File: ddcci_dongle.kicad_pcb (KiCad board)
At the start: 4 copper layers, 31 x 64 mm, 52 parts, among them U1 PCA9306, U10 TPD1E05U06DPY, U11 TPD1E05U06DPY, U12 TPD1E05U06DPY, U2 NCP1117-3.3_SOT223, U3 RP2040, U4 W25Q128JVPIQ, U6 TPD1E05U06DPY, U8 TPD1E05U06DPY, U9 TPD1E05U06DPY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

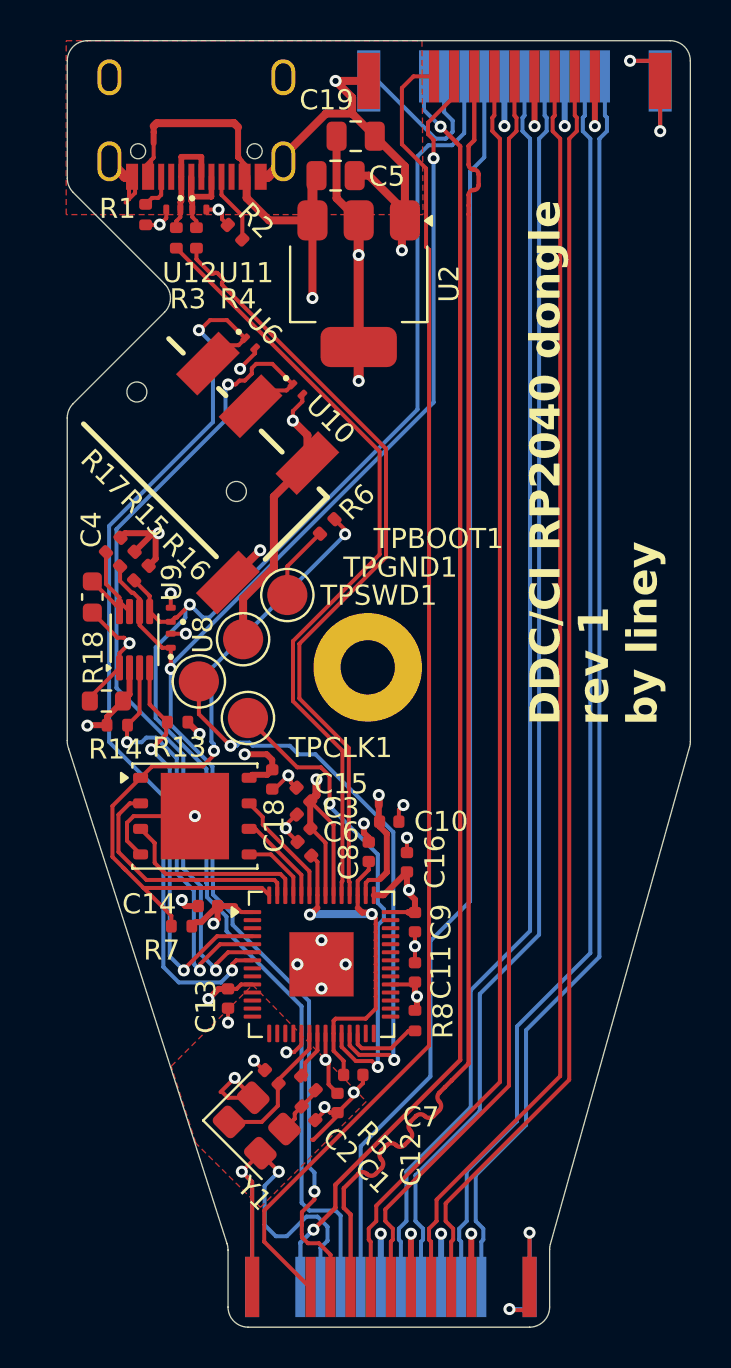
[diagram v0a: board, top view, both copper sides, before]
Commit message: Final update before rev1 production
* Update LCSC PN# fields
* Add ground to layer 3 (3.3v has been reduced to a polygon)
* Remove the antennas on the right (behind HDMI lanes)
* Remove the ground plane "capacitor" under the XTAL
* Prettier testpoint labels
* Prettier tracks overall

Signed-off-by: Elvira Khabirova <lineprinter0@gmail.com>
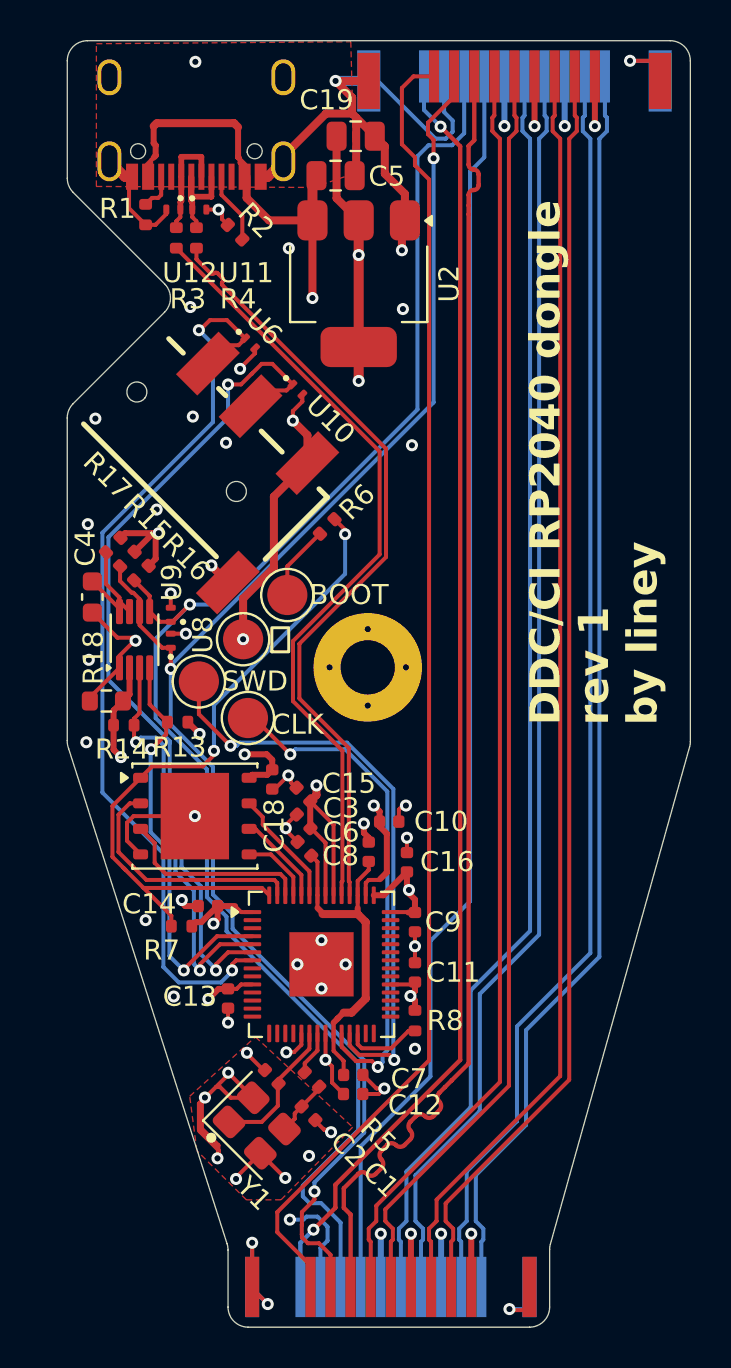
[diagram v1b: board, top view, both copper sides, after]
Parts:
- moved C12 0.90 mm to (126.2, 125.8), turned to 0 degrees
- moved R14 0.32 mm to (114.8, 107.4)
- moved R5 0.25 mm to (124.2, 125.0)
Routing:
- net GND: track 132.8 -> 120.2 mm, vias 33 -> 56
- net +1V1: track 19.9 -> 17.1 mm, vias 2 -> 0
- net /DISPLAY_SCK: track 76.9 -> 78.9 mm
- net Net-(U3-SWCLK): track 23.9 -> 25.4 mm
- net /DISPLAY_SDA: track 77.8 -> 79.1 mm
- net Net-(U3-SWD): track 28.4 -> 29.6 mm
- net +3V3: track 59.4 -> 58.5 mm
- net Net-(HDMI1-+5VPower): track 66.4 -> 65.9 mm
- net /SHIFTED_DISPLAY_SCK: track 21.3 -> 20.8 mm
- added copper zone on In2.Cu, net GND
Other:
- board text added: "BOOT"
- board text added: "CLK"
- board text added: "SWD"
- board text added: "⏚"

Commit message: Fix SDA/SCL for the monitor. Bump to rev2
Signed-off-by: Elvira Khabirova <lineprinter0@gmail.com>
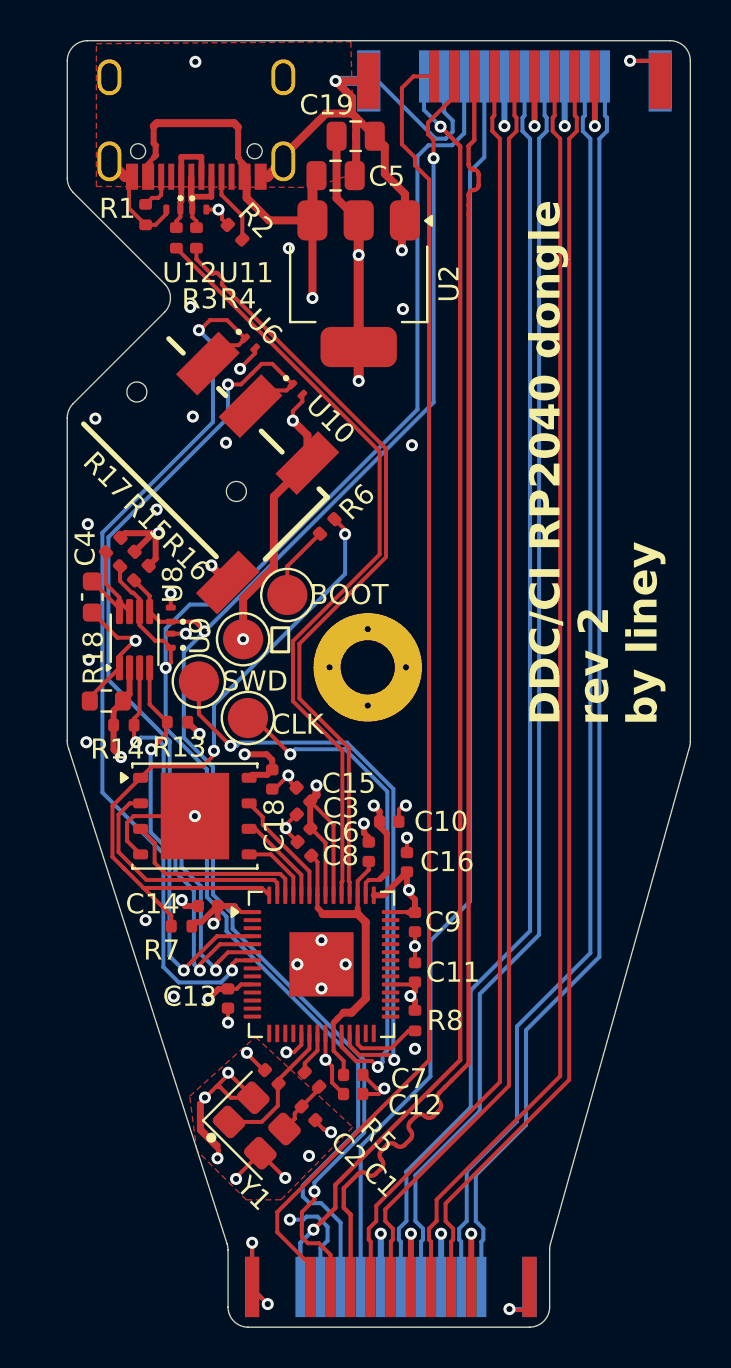
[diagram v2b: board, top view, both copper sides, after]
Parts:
- moved U8 1.30 mm to (117.2, 101.9)
- moved U9 1.29 mm to (117.2, 103.2)
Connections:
- HDMI1 pad 15: /DISPLAY_SDA -> /DISPLAY_SCK
- HDMI1 pad 16: /DISPLAY_SCK -> /DISPLAY_SDA
- U5 pad 15: /DISPLAY_SDA -> /DISPLAY_SCK
- U5 pad 16: /DISPLAY_SCK -> /DISPLAY_SDA
- U8 pad 1: /DISPLAY_SCK -> /DISPLAY_SDA
- U9 pad 1: /DISPLAY_SDA -> /DISPLAY_SCK
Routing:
- net /DISPLAY_SDA: track 79.1 -> 77.1 mm, vias 1 -> 3
- net /DISPLAY_SCK: track 78.9 -> 80.7 mm, vias 3 -> 1
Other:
- board text added: "DDC/CI RP2040 dongle rev 2 by liney"
- board text removed: "DDC/CI RP2040 dongle rev 1 by liney"

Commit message: WIP: Make the board narrower
Todo: make the board shorter

Signed-off-by: Elvira Khabirova <lineprinter0@gmail.com>
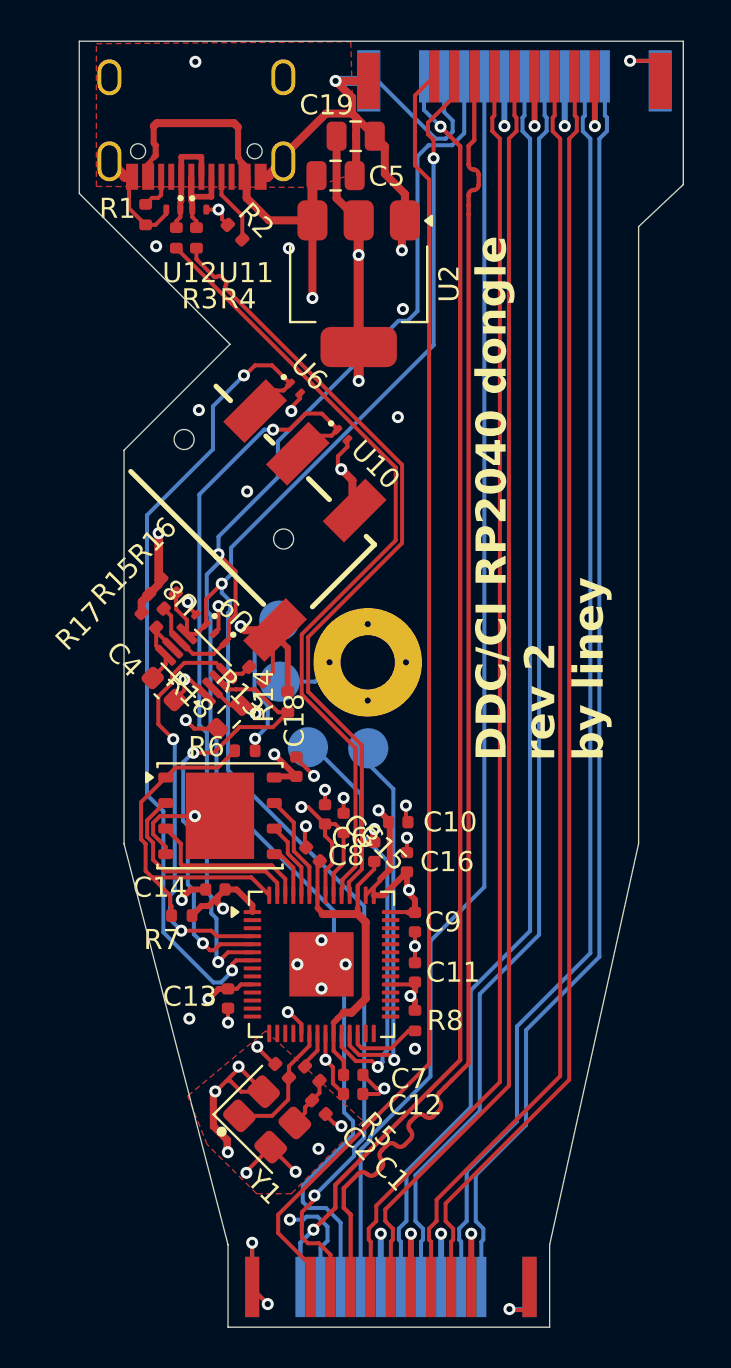
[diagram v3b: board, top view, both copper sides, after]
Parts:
- TPBOOT1, TPCLK1, TPGND1, TPSWD1: moved to B.Cu
- moved R6 11.9 mm to (120.8, 108.7), turned to 0 degrees
- moved TPSWD1 9.06 mm to (127.0, 108.5)
- moved R14 8.24 mm to (123.0, 106.2), turned to -90 degrees
- moved R18 6.16 mm to (120.1, 107.0), turned to -135 degrees
- moved C4 5.79 mm to (116.8, 105.6), turned to -45 degrees
- moved R13 4.59 mm to (121.4, 104.9), turned to 135 degrees
- moved R17 4.15 mm to (116.1, 102.2), turned to -45 degrees
- moved CN1 3.33 mm to (121.8, 97.2)
- moved TPCLK1 3.32 mm to (124.0, 108.5)
- moved U1 3.30 mm to (118.4, 104.4), turned to 135 degrees
- moved U6 3.17 mm to (123.3, 90.7)
- moved U10 3.17 mm to (125.7, 93.0)
- moved TPGND1 2.79 mm to (122.6, 105.2)
- moved R15 2.56 mm to (116.4, 101.2), turned to -45 degrees
- moved C15 2.45 mm to (125.8, 112.3), turned to 90 degrees
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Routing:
- net /QSPI_SS: track 34.5 -> 18.2 mm, vias 2 -> 0
- net GND: track 120.2 -> 109.6 mm, vias 56 -> 52
- net Net-(U3-SWD): track 29.6 -> 19.2 mm, vias 2 -> 1
- net /PERIPHERAL_SDA: track 42.8 -> 36.7 mm
- net /PERIPHERAL_SCK: track 46.2 -> 41.4 mm
- net Net-(U3-SWCLK): track 25.4 -> 20.8 mm, vias 2 -> 1
- net /~{USB_BOOT}: track 3.72 -> 7.52 mm, vias 0 -> 1
- net /QSPI_SD1: track 12.3 -> 10.6 mm
- net Net-(U1-EN): track 5.99 -> 4.32 mm
- net /SHIFTED_DISPLAY_SCK: track 20.8 -> 22.4 mm
- net +3V3: track 58.5 -> 60.0 mm, vias 13 -> 12
- net /QSPI_SD2: track 9.62 -> 8.40 mm
- net /SHIFTED_DISPLAY_SDA: track 20.5 -> 21.8 mm
- net Net-(HDMI1-+5VPower): track 65.9 -> 64.7 mm
- net VBUS: track 42.8 -> 43.9 mm
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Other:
- board size 31 x 64 mm -> 30.1 x 64 mm

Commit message: Make the board shorter for rev2
Signed-off-by: Elvira Khabirova <lineprinter0@gmail.com>
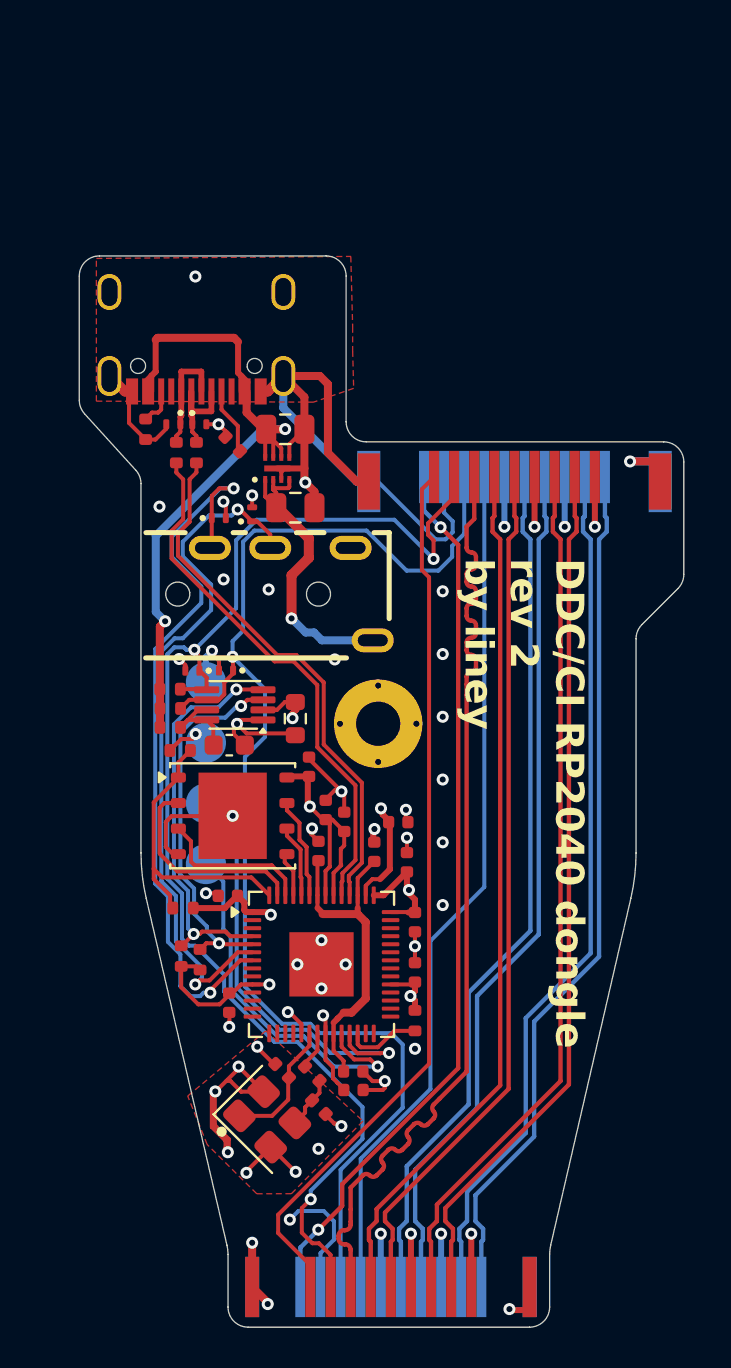
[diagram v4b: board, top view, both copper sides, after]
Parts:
- removed U2: NCP1117-3.3_SOT223, Package_TO_SOT_SMD:SOT-223-3_TabPin2
- added U7: ~, ddcci_dongle_parts:XDFN-8_L1.6-W1.2-P0.40-BL-EP, F.Cu at (122.5, 94.6)
- C19, C5: value 10uF -> 1uF X5R/X7R
- CN1: footprint ddcci_dongle_parts:AUDIO-SMD_PJ-320D-1 -> ddcci_dongle_parts:AUDIO-TH_PJ-320A-4P-DIP
- H1: footprint MountingHole:MountingHole_2.7mm_M2.5_Pad -> MountingHole:MountingHole_2.2mm_M2_Pad
- moved U5 19.9 mm to (134.2, 95.2)
- moved C19 18.7 mm to (123.3, 96.6)
- moved R13 14.5 mm to (117.7, 118.9), turned to 90 degrees
- moved R14 13.5 mm to (118.6, 119.1), turned to 90 degrees
- moved C5 12.9 mm to (122.8, 92.7)
- moved R3 10.7 mm to (117.4, 93.8)
- moved R4 10.7 mm to (118.4, 93.8)
- moved R1 10.7 mm to (115.9, 92.7)
- moved U11 10.7 mm to (118.6, 92.4)
- moved U12 10.7 mm to (117.3, 92.4)
- moved USB1 10.7 mm to (118.4, 88.3)
- moved R2 10.5 mm to (120.2, 93.4)
- moved TPSWD1 8.53 mm to (118.9, 111.3), turned to 0 degrees
- moved TPCLK1 7.71 mm to (118.9, 114.3), turned to 0 degrees
- moved U6 7.49 mm to (119.5, 97.1), turned to 0 degrees
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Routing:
- net Net-(HDMI1-+5VPower): track 64.7 -> 44.5 mm
- net /HDMI_DP_HECN: track 64.3 -> 44.3 mm
- net /HDMI_DP_CKN: track 63.2 -> 43.2 mm
- net /HDMI_DP_D2P: track 63.2 -> 43.2 mm
- net /HDMI_DP_D0N: track 63.2 -> 43.2 mm
- net /HDMI_DP_D2N: track 63.2 -> 43.2 mm
- net /HDMI_DP_D1P: track 63.2 -> 43.2 mm
- net /HDMI_DP_D1N: track 63.2 -> 43.2 mm
- net /HDMI_DP_D0P: track 63.2 -> 43.2 mm
- net /HDMI_DP_CKP: track 63.2 -> 43.2 mm
- net Net-(HDMI1-CEC): track 62.8 -> 42.8 mm
- net /HDMI_DP_HECP: track 65.5 -> 47.0 mm
- net /DISPLAY_SCK: track 81.5 -> 66.3 mm
- net /USB_RP2040_P: track 40.0 -> 26.5 mm
- net /USB_RP2040_N: track 40.0 -> 26.5 mm
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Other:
- board size 30.1 x 64 mm -> 30.1 x 53.3 mm
- board text added: "GND"
- board text added: "JLC04161H-7628 90ohm diffpair non-coplanar (USB) Trace Width 0.1994 Trace Spacing 0.1190 100ohm diffpair non-coplanar (HDMI) Trace Width 0.2182 Trace Spacing 0.2000"
- board text removed: "JLC04161H-7628 90ohm diffpair non-coplanar (USB) Trace Width 0.2840 Trace Spacing 0.2000 Trace Width 0.1994 Trace Spacing 0.1190 100ohm diffpair non-coplanar (HDMI) Trace Width 0.2182 Trace Spacing 0.2000 Trace Width 0.1425 Trace Spacing 0.1200"
- board text removed: "⏚"

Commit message: Follow serpentine recommendations
> When a serpentine section is used to match one length to another, ...
> the length of each jog must be at least three times the trace width.
> The maximum distance between traces in a serpentine section should be less
> than two times the distance between traces in a non-serpentine section.

Signed-off-by: Elvira Khabirova <lineprinter0@gmail.com>
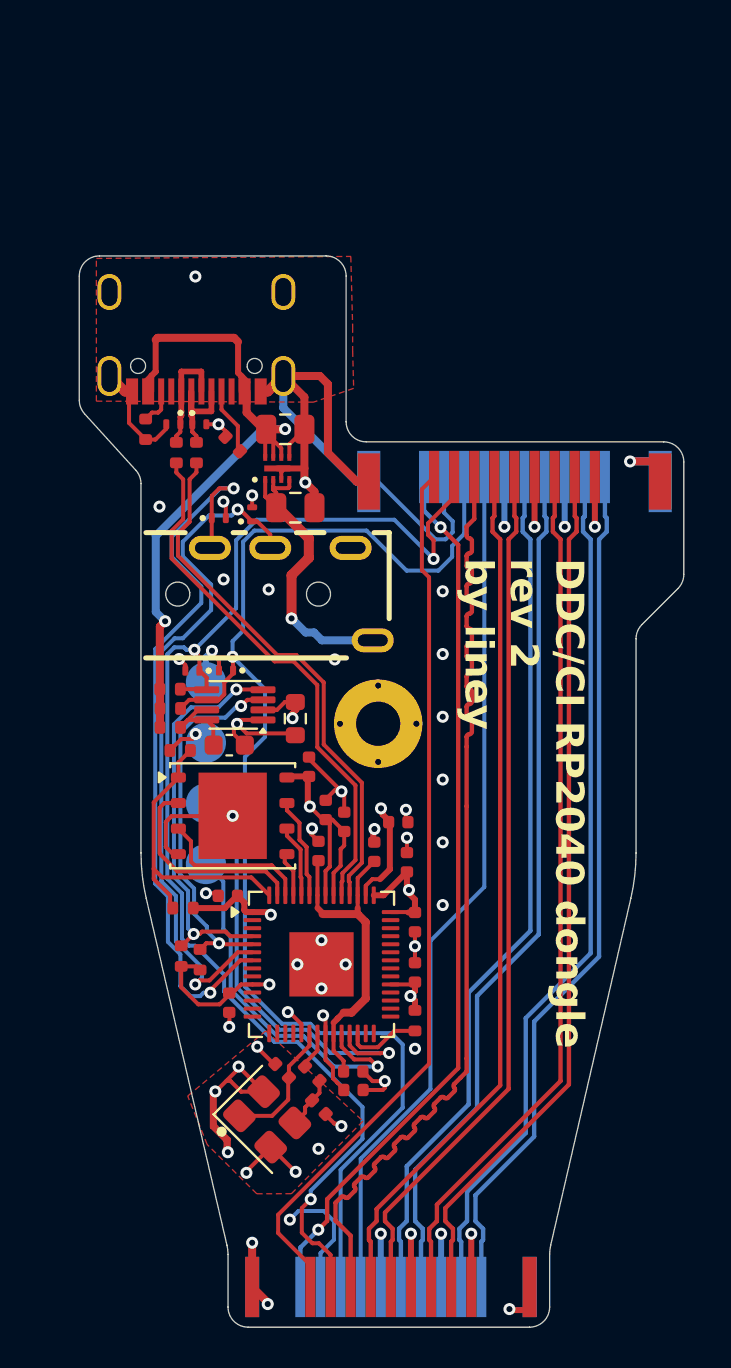
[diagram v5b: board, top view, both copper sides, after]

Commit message: Make the board even shorter
Signed-off-by: Elvira Khabirova <lineprinter0@gmail.com>
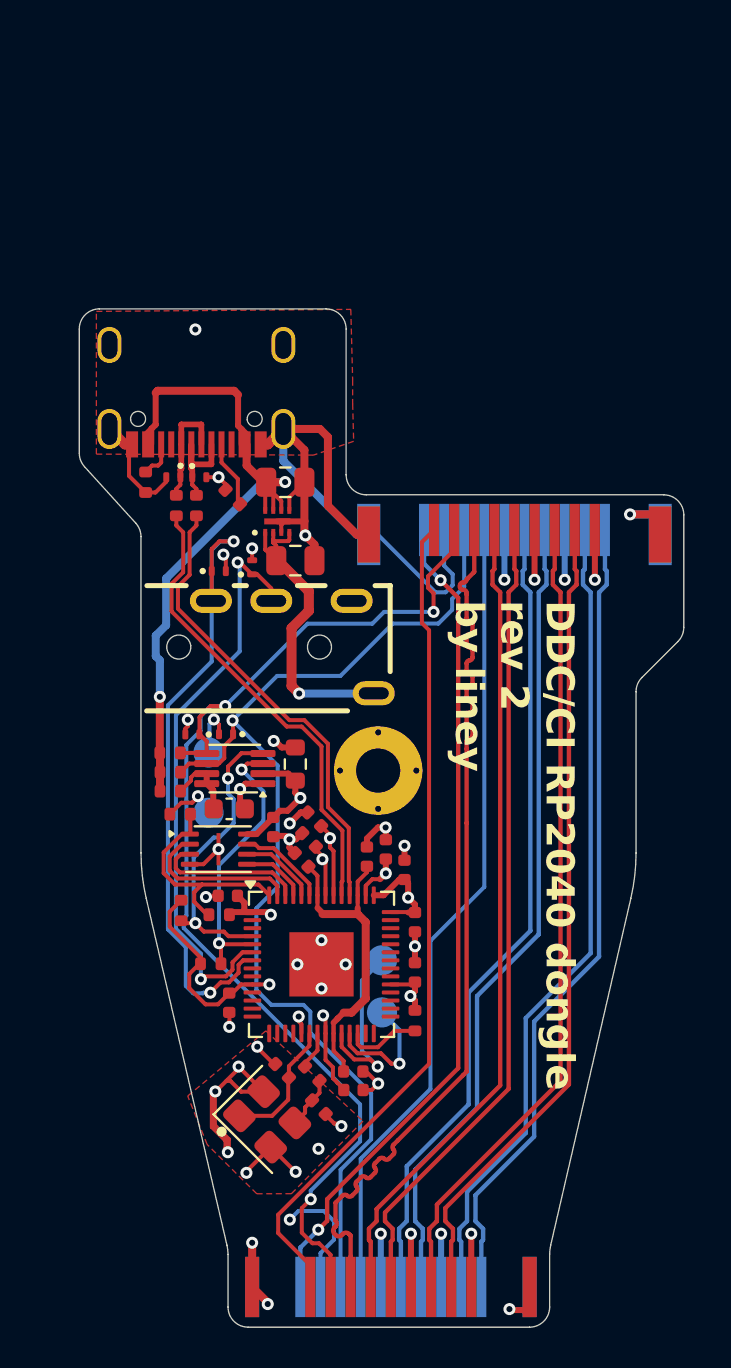
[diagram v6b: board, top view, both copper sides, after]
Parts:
- TPBOOT1, TPCLK1, TPGND1, TPSWD1: footprint TestPoint:TestPoint_Pad_D2.0mm -> TestPoint:TestPoint_Pad_D1.5mm
- U4: value W25Q128JVPIQ -> W25Q16JVUXIQ; footprint Package_SON:WSON-8-1EP_6x5mm_P1.27mm_EP3.4x4.3mm -> Package_SON:Winbond_USON-8-1EP_3x2mm_P0.5mm_EP0.2x1.6mm
- moved TPSWD1 13.6 mm to (127.7, 121.7)
- moved TPCLK1 9.98 mm to (127.7, 119.1)
- moved TPGND1 3.50 mm to (119.0, 108.8)
- moved C18 3.49 mm to (122.2, 112.5), turned to -90 degrees
- moved TPBOOT1 3.49 mm to (119.0, 111.8)
- moved C4 3.17 mm to (120.1, 111.6)
- moved R15 3.17 mm to (117.1, 109.7)
- moved R16 3.17 mm to (117.1, 108.8)
- moved R6 3.17 mm to (117.6, 111.8)
- moved U1 3.17 mm to (120.3, 109.6)
- moved U8 3.17 mm to (118.2, 107.9)
- moved R17 3.17 mm to (117.1, 110.7)
- moved U9 3.17 mm to (119.9, 107.9)
- moved CN1 2.64 mm to (123.2, 103.5)
- moved C19 2.63 mm to (123.3, 99.2)
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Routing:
- net Net-(U3-SWD): track 21.4 -> 6.36 mm
- net /DISPLAY_SCK: track 66.3 -> 55.4 mm
- net Net-(U3-SWCLK): track 18.5 -> 8.89 mm
- net /DISPLAY_SDA: track 65.8 -> 57.6 mm
- net GND: track 113.9 -> 105.7 mm, vias 51 -> 40
- net /PERIPHERAL_SDA: track 35.1 -> 28.8 mm
- net /SHIFTED_DISPLAY_SDA: track 19.9 -> 14.8 mm
- net /SHIFTED_DISPLAY_SCK: track 18.8 -> 13.9 mm
- net /PERIPHERAL_SCK: track 37.0 -> 32.5 mm
- net /QSPI_SS: track 15.3 -> 11.4 mm
- net +3V3: track 59.9 -> 56.4 mm, vias 9 -> 10
- net /USB_RP2040_P: track 26.5 -> 23.2 mm
- net /USB_RP2040_N: track 26.5 -> 23.2 mm
- net Net-(HDMI1-+5VPower): track 44.5 -> 41.8 mm
- net /HDMI_DP_D1P: track 43.2 -> 40.6 mm
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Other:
- board size 30.1 x 53.3 mm -> 30.1 x 50.7 mm
